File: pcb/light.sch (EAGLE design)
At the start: 4 parts, among them J3 FFC3B07-05-T, U1 TEMT6000

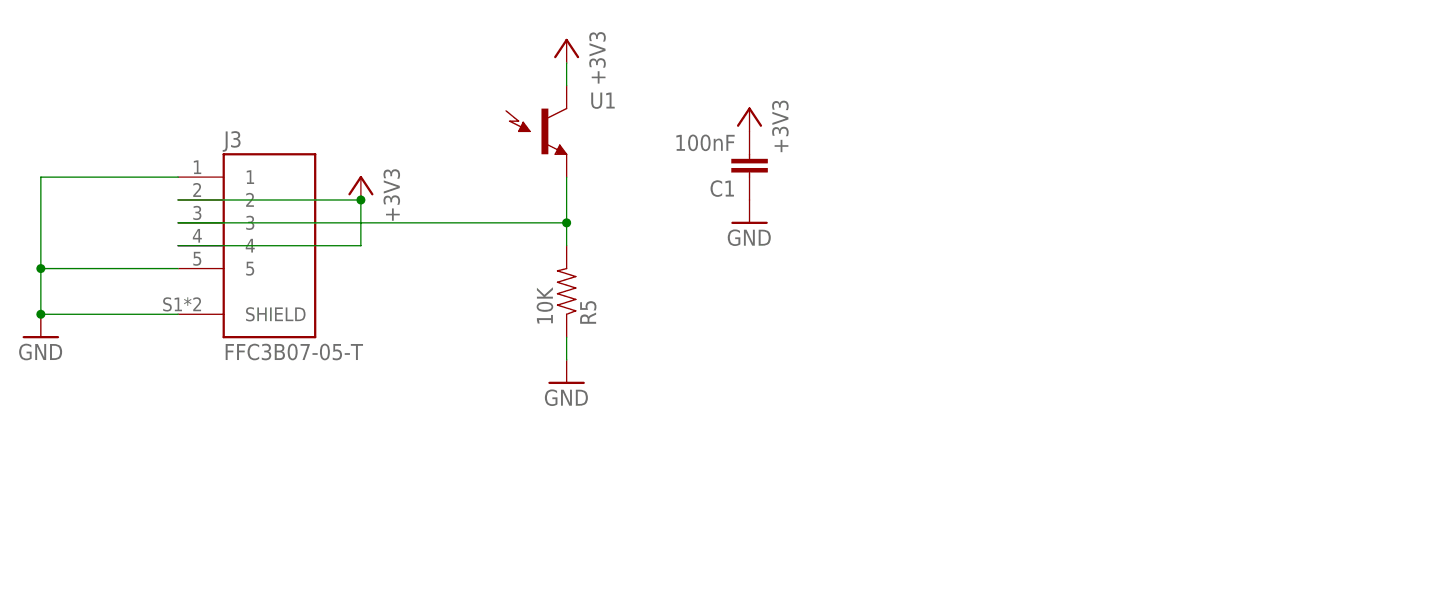
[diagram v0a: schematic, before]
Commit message: added website
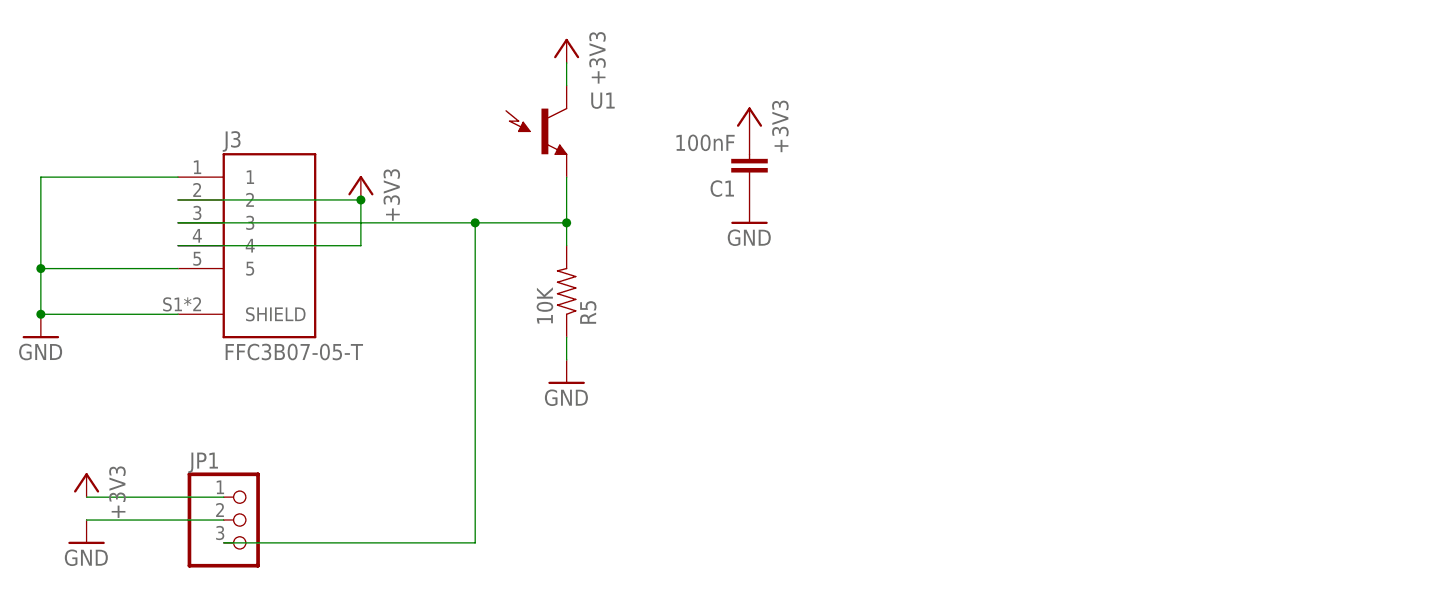
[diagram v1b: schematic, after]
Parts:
- added JP1: (no value), adafruit_changed:PINHD-1X3CB
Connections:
- net +3V3: now also JP1.1
- net GND: now also JP1.2
- net S: now also JP1.3
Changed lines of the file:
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@@
 <part name="+3V2" library="supply1" library_urn="urn:adsk.eagle:library:371" deviceset="+3V3" device=""/>
 <part name="GND3" library="SparkFun" deviceset="GND" device=""/>
+<part name="JP1" library="adafruit_changed" deviceset="PINHD-1X3" device="CB"/>
+<part name="GND4" library="SparkFun" deviceset="GND" device=""/>
+<part name="+3V3" library="supply1" library_urn="urn:adsk.eagle:library:371" deviceset="+3V3" device=""/>
 </parts>
 <sheets>
@@
 <attribute name="VALUE" x="38.1" y="40.64" size="1.778" layer="96"/>
 </instance>
+<instance part="JP1" gate="A" x="-15.24" y="10.16" smashed="yes">
+<attribute name="NAME" x="-21.59" y="15.875" size="1.778" layer="95"/>
+<attribute name="VALUE" x="-21.59" y="2.54" size="1.778" layer="96"/>
+</instance>
+<instance part="GND4" gate="1" x="-33.02" y="7.62" smashed="yes">
+<attribute name="VALUE" x="-35.56" y="5.08" size="1.778" layer="96"/>
+</instance>
+<instance part="+3V3" gate="G$1" x="-33.02" y="15.24" smashed="yes" rot="MR0">
+<attribute name="VALUE" x="-30.48" y="10.16" size="1.778" layer="96" rot="MR90"/>
+</instance>
 </instances>
 <busses>
@@
 <pinref part="U1" gate="G$1" pin="E1"/>
 <pinref part="J3" gate="G$1" pin="3"/>
-<wire x1="-22.86" y1="43.18" x2="20.32" y2="43.18" width="0.1524" layer="91"/>
+<wire x1="-22.86" y1="43.18" x2="10.16" y2="43.18" width="0.1524" layer="91"/>
 <pinref part="R5" gate="G$1" pin="2"/>
+<wire x1="10.16" y1="43.18" x2="20.32" y2="43.18" width="0.1524" layer="91"/>
 <wire x1="20.32" y1="43.18" x2="20.32" y2="40.64" width="0.1524" layer="91"/>
 <junction x="20.32" y="43.18"/>
+<pinref part="JP1" gate="A" pin="3"/>
+<wire x1="10.16" y1="43.18" x2="10.16" y2="7.62" width="0.1524" layer="91"/>
+<wire x1="10.16" y1="7.62" x2="-17.78" y2="7.62" width="0.1524" layer="91"/>
+<junction x="10.16" y="43.18"/>
 </segment>
 </net>
@@
 <pinref part="GND3" gate="1" pin="GND"/>
 </segment>
+<segment>
+<pinref part="JP1" gate="A" pin="2"/>
+<pinref part="GND4" gate="1" pin="GND"/>
+<wire x1="-17.78" y1="10.16" x2="-33.02" y2="10.16" width="0.1524" layer="91"/>
+</segment>
 </net>
 <net name="+3V3" class="0">
@@
 <pinref part="+3V2" gate="G$1" pin="+3V3"/>
 </segment>
+<segment>
+<pinref part="JP1" gate="A" pin="1"/>
+<pinref part="+3V3" gate="G$1" pin="+3V3"/>
+<wire x1="-17.78" y1="12.7" x2="-33.02" y2="12.7" width="0.1524" layer="91"/>
+</segment>
 </net>

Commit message: cleanup PCB files
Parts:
- removed JP1: (no value), adafruit_changed:PINHD-1X3CB
- added U$1: LS_VERT, apricot:LS_VERT
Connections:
- net +3V3: now also U$1.B1, U$1.B2; no longer JP1.1
- net GND: now also U$1.T1, U$1.T2; no longer JP1.2
- net S: now also U$1.B3, U$1.B4, U$1.T3, U$1.T4; no longer JP1.3
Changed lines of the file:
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@@
 <part name="+3V2" library="supply1" library_urn="urn:adsk.eagle:library:371" deviceset="+3V3" device=""/>
 <part name="GND3" library="SparkFun" deviceset="GND" device=""/>
-<part name="JP1" library="adafruit_changed" deviceset="PINHD-1X3" device="CB"/>
 <part name="GND4" library="SparkFun" deviceset="GND" device=""/>
-<part name="+3V3" library="supply1" library_urn="urn:adsk.eagle:library:371" deviceset="+3V3" device=""/>
+<part name="U$1" library="apricot" deviceset="LS_VERT" device=""/>
+<part name="+3V4" library="supply1" library_urn="urn:adsk.eagle:library:371" deviceset="+3V3" device=""/>
 </parts>
 <sheets>
@@
 <attribute name="VALUE" x="38.1" y="40.64" size="1.778" layer="96"/>
 </instance>
-<instance part="JP1" gate="A" x="-15.24" y="10.16" smashed="yes">
-<attribute name="NAME" x="-21.59" y="15.875" size="1.778" layer="95"/>
-<attribute name="VALUE" x="-21.59" y="2.54" size="1.778" layer="96"/>
+<instance part="GND4" gate="1" x="58.42" y="35.56" smashed="yes">
+<attribute name="VALUE" x="55.88" y="33.02" size="1.778" layer="96"/>
 </instance>
-<instance part="GND4" gate="1" x="-33.02" y="7.62" smashed="yes">
-<attribute name="VALUE" x="-35.56" y="5.08" size="1.778" layer="96"/>
-</instance>
-<instance part="+3V3" gate="G$1" x="-33.02" y="15.24" smashed="yes" rot="MR0">
-<attribute name="VALUE" x="-30.48" y="10.16" size="1.778" layer="96" rot="MR90"/>
+<instance part="U$1" gate="G$1" x="101.6" y="20.32" smashed="yes"/>
+<instance part="+3V4" gate="G$1" x="109.22" y="40.64" smashed="yes" rot="MR0">
+<attribute name="VALUE" x="111.76" y="35.56" size="1.778" layer="96" rot="MR90"/>
 </instance>
 </instances>
@@
 <pinref part="U1" gate="G$1" pin="E1"/>
 <pinref part="J3" gate="G$1" pin="3"/>
-<wire x1="-22.86" y1="43.18" x2="10.16" y2="43.18" width="0.1524" layer="91"/>
+<wire x1="-22.86" y1="43.18" x2="20.32" y2="43.18" width="0.1524" layer="91"/>
 <pinref part="R5" gate="G$1" pin="2"/>
-<wire x1="10.16" y1="43.18" x2="20.32" y2="43.18" width="0.1524" layer="91"/>
 <wire x1="20.32" y1="43.18" x2="20.32" y2="40.64" width="0.1524" layer="91"/>
 <junction x="20.32" y="43.18"/>
-<pinref part="JP1" gate="A" pin="3"/>
-<wire x1="10.16" y1="43.18" x2="10.16" y2="7.62" width="0.1524" layer="91"/>
-<wire x1="10.16" y1="7.62" x2="-17.78" y2="7.62" width="0.1524" layer="91"/>
-<junction x="10.16" y="43.18"/>
+<wire x1="20.32" y1="43.18" x2="33.02" y2="43.18" width="0.1524" layer="91"/>
+<wire x1="33.02" y1="43.18" x2="33.02" y2="22.86" width="0.1524" layer="91"/>
+<pinref part="U$1" gate="G$1" pin="B3"/>
+<pinref part="U$1" gate="G$1" pin="B4"/>
+<wire x1="99.06" y1="27.94" x2="99.06" y2="22.86" width="0.1524" layer="91"/>
+<wire x1="99.06" y1="22.86" x2="99.06" y2="10.16" width="0.1524" layer="91"/>
+<wire x1="99.06" y1="10.16" x2="68.58" y2="10.16" width="0.1524" layer="91"/>
+<junction x="99.06" y="22.86"/>
+<pinref part="U$1" gate="G$1" pin="T3"/>
+<pinref part="U$1" gate="G$1" pin="T4"/>
+<wire x1="68.58" y1="27.94" x2="68.58" y2="22.86" width="0.1524" layer="91"/>
+<wire x1="68.58" y1="10.16" x2="68.58" y2="22.86" width="0.1524" layer="91"/>
+<junction x="68.58" y="22.86"/>
+<wire x1="33.02" y1="22.86" x2="68.58" y2="22.86" width="0.1524" layer="91"/>
 </segment>
 </net>
@@
 </segment>
 <segment>
-<pinref part="JP1" gate="A" pin="2"/>
 <pinref part="GND4" gate="1" pin="GND"/>
-<wire x1="-17.78" y1="10.16" x2="-33.02" y2="10.16" width="0.1524" layer="91"/>
+<pinref part="U$1" gate="G$1" pin="T1"/>
+<wire x1="58.42" y1="38.1" x2="68.58" y2="38.1" width="0.1524" layer="91"/>
+<pinref part="U$1" gate="G$1" pin="T2"/>
+<wire x1="68.58" y1="33.02" x2="68.58" y2="38.1" width="0.1524" layer="91"/>
+<junction x="68.58" y="38.1"/>
 </segment>
 </net>
@@
 </segment>
 <segment>
-<pinref part="JP1" gate="A" pin="1"/>
-<pinref part="+3V3" gate="G$1" pin="+3V3"/>
-<wire x1="-17.78" y1="12.7" x2="-33.02" y2="12.7" width="0.1524" layer="91"/>
+<pinref part="U$1" gate="G$1" pin="B1"/>
+<wire x1="99.06" y1="38.1" x2="109.22" y2="38.1" width="0.1524" layer="91"/>
+<pinref part="+3V4" gate="G$1" pin="+3V3"/>
+<pinref part="U$1" gate="G$1" pin="B2"/>
+<wire x1="99.06" y1="33.02" x2="99.06" y2="38.1" width="0.1524" layer="91"/>
+<junction x="99.06" y="38.1"/>
 </segment>
 </net>
